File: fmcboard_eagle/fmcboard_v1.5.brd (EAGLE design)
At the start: 147 x 74 mm, 174 parts, among them IC1 OPA699ID, IC10 LTC6229IMS8E#TRPBF, IC11 7805TV, IC12 SN74AUC2G66DCTR, IC13 SN74AUC2G66DCTR, IC14 SN74AUC2G66DCTR, IC15 SN74AUC2G66DCTR, IC16 DAC7578SPWR, IC17 SN74AUC2G66DCTR, IC18 SN74AUC2G66DCTR, IC19 SN74AUC2G66DCTR, IC2 DAC7578SPWR, IC20 SN74AUC2G66DCTR, IC21 74LVC2G06GW,125, IC22 74LVC2G06GW,125, IC23 74LVC2G06GW,125, IC24 74LVC2G06GW,125, IC3 LTC6229IMS8E#TRPBF, IC4 LTC6229IMS8E#TRPBF, IC5 LM358, IC6 OPA699ID, IC7 OPA699ID, IC8 LTC6229IMS8E#TRPBF, IC9 LTC6229IMS8E#TRPBF, J1 8pin, J10 8pin, J12 4p-2.54, J2 ASP-134604-01, J3 4p-2.54, J4 4p-2.54, J5 8pin, J6 4p-2.54, J7 4p-2.54, J8 4p-2.54, J9 8pin, U1 TXS0108EPWR, U2 STMICROELECTRONICS_L7905ACVST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

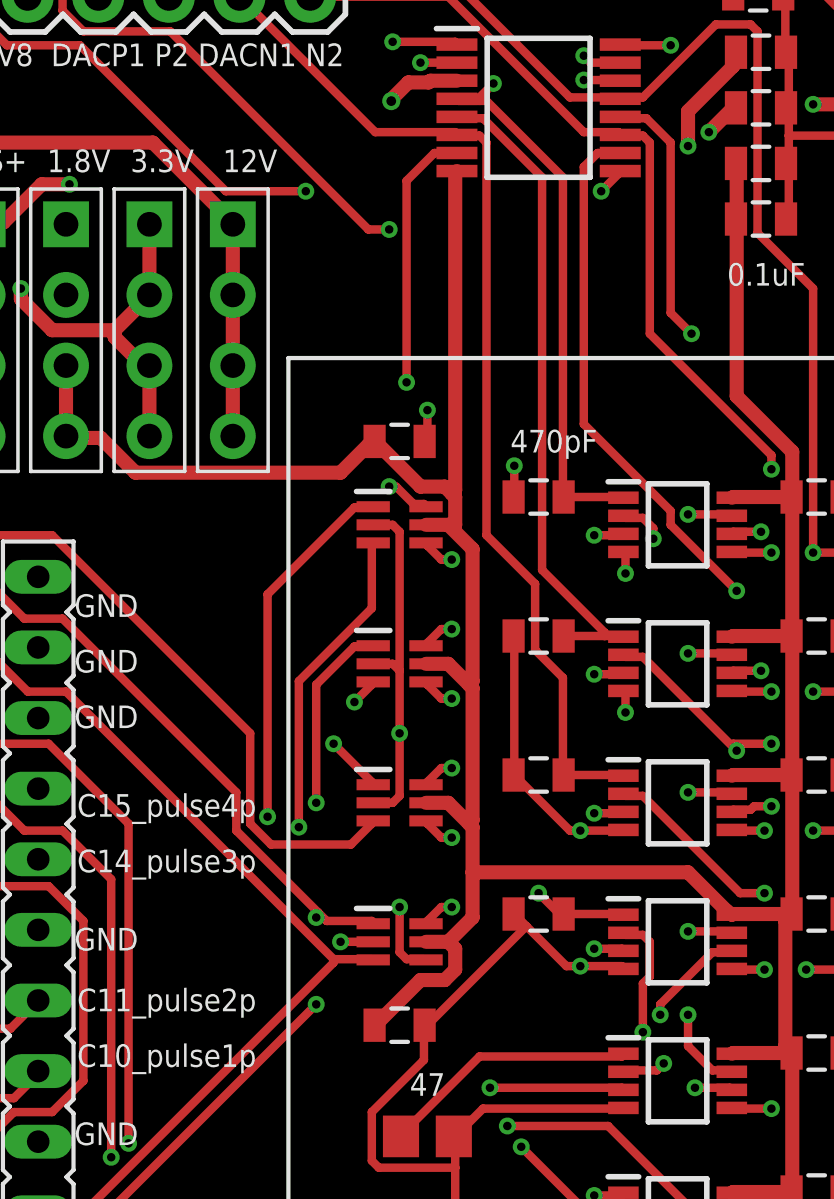
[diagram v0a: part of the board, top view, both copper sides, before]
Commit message: Switch to 74LVC2GU04 inverters
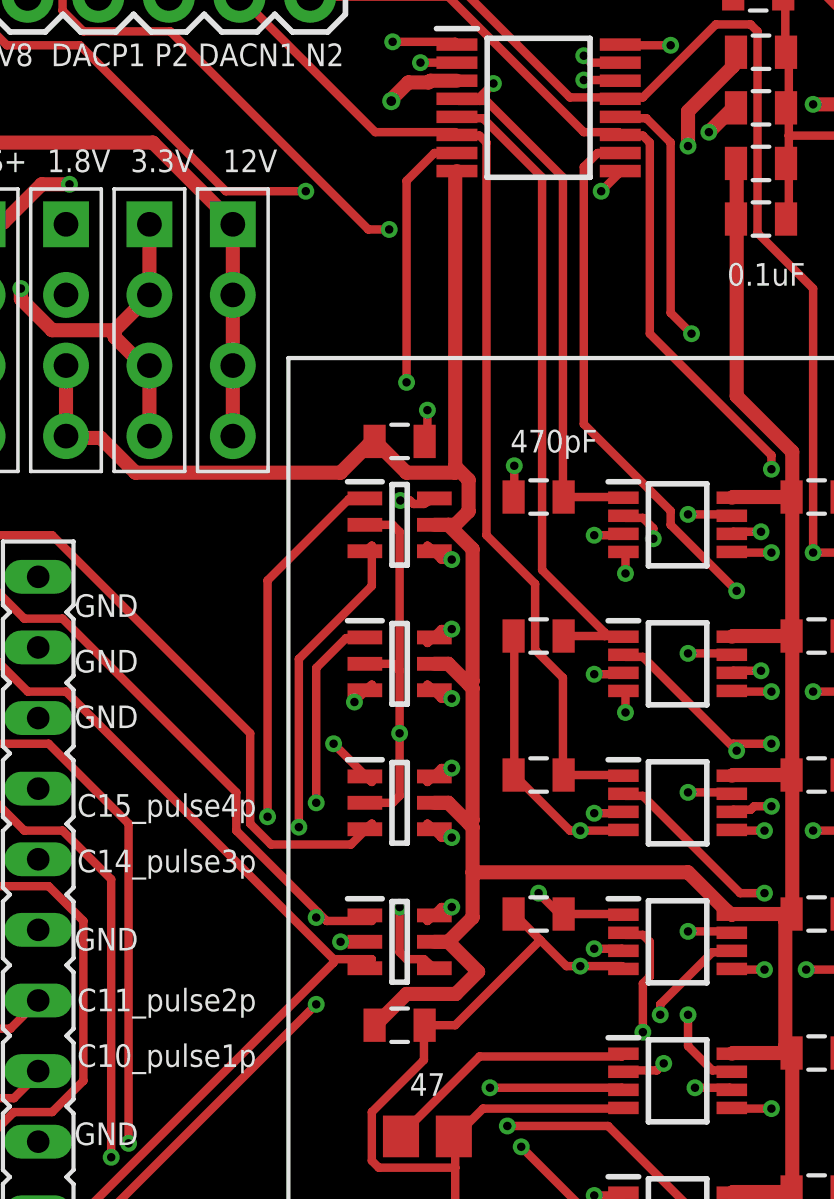
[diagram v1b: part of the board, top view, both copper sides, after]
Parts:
- IC21, IC22, IC23, IC24: value 74LVC2G06GW,125 -> 74LVC2GU04GV,125; device 74LVC2G06GW_125:SOT65P210X110-6N -> 74LVC2GU04GV_125:SOT95P275X110-6N
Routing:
- net C10N: track 14.4 -> 13.5 mm
- net GND: track 397.7 -> 398.6 mm

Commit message: Revert "Switch to 74LVC2GU04 inverters"
This reverts commit 0d5c0f9254668030431faa83bc2596f2b624104f.
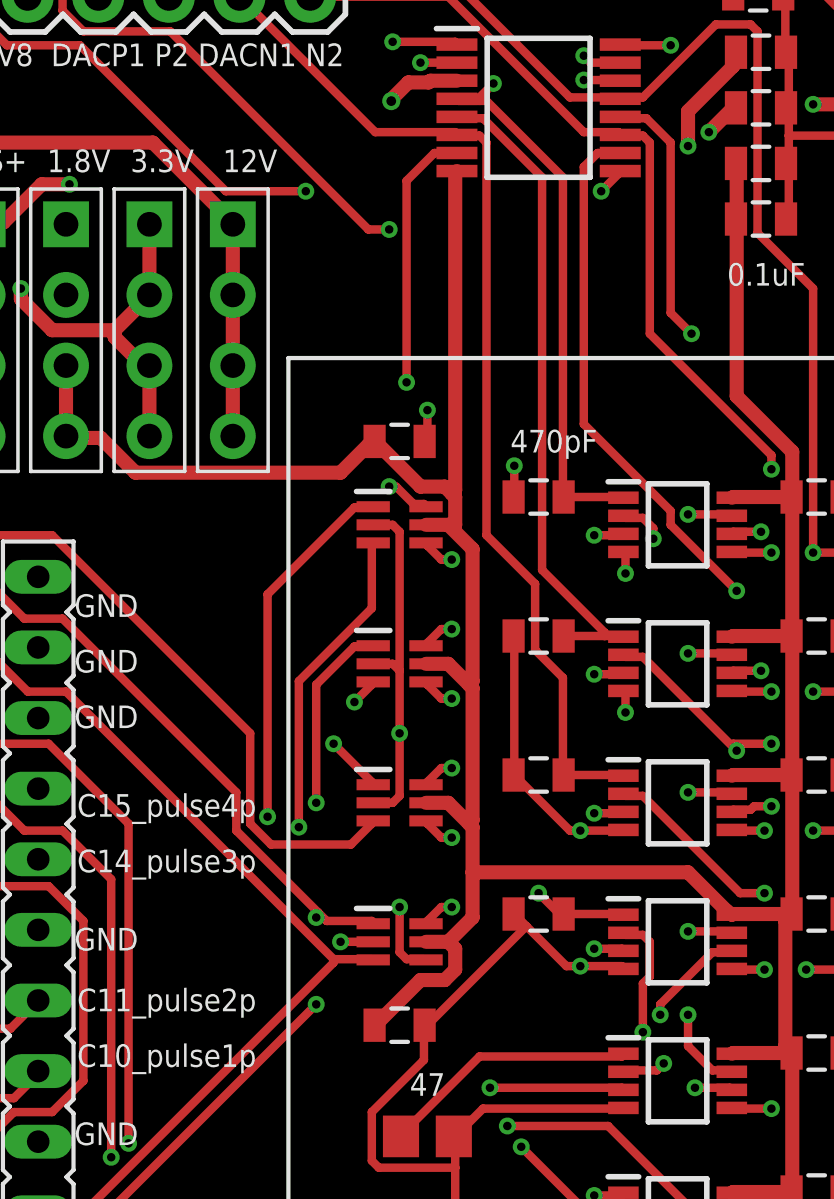
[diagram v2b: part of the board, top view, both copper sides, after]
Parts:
- IC21, IC22, IC23, IC24: value 74LVC2GU04GV,125 -> 74LVC2G06GW,125; device 74LVC2GU04GV_125:SOT95P275X110-6N -> 74LVC2G06GW_125:SOT65P210X110-6N
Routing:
- net C10N: track 13.5 -> 14.4 mm
- net GND: track 398.6 -> 397.7 mm
